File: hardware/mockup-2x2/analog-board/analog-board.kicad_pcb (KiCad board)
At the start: 4 copper layers, 100 x 62 mm, 135 parts, among them J1 12V, J2 COIL JOINT, J4 MCU, J5 PI ZERO, Q1 AO3401A, Q11 AO3400A, Q12 AO3400A, Q13 AO3400A, Q14 AO3400A, Q2 AO3400A, Q21 AO3401A, Q22 AO3401A, Q23 AO3401A, Q24 AO3401A, U1 TPS62150, U2 LP2985-5.0, U3 74HC4052, U4 AD8421, U5 OPA2810, U6 OPA2810, U7 ADuM1201

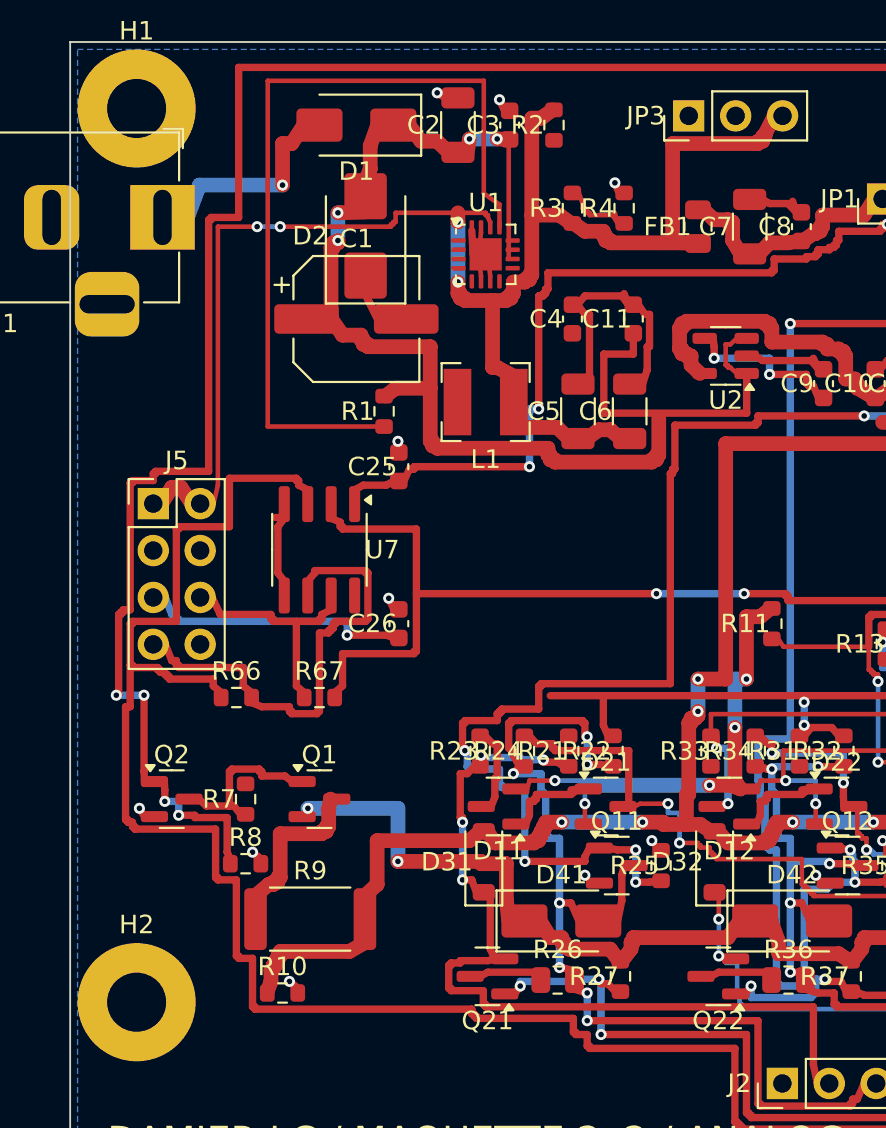
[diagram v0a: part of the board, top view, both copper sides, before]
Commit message: Carte analogique de reference : 18 restes contre 23, artefacts a jour
Generation finale avec les trois seeds nord ouest : 464 pistes, 242
vias, DRC zero, BUCK_SS, BUCK_DEF et la broche isolateur PI_3V3
desormais fermes sans deplacement d'autres nets. Gerbers, placements
JLC et rendu regeneres ; le README de la carte porte la liste de
finition exacte (quatre liaisons jamais routees et les morceaux a
raccorder) et la note de methode sur la saturation locale du routage.
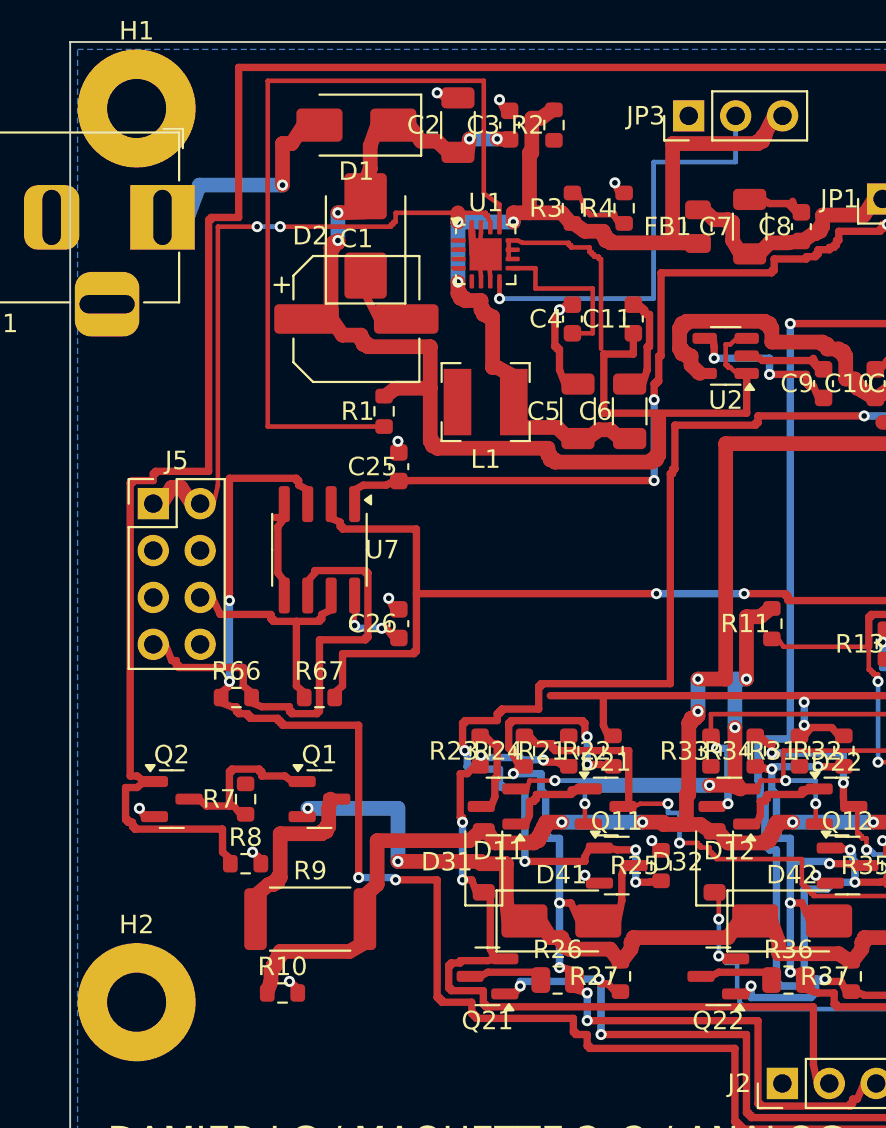
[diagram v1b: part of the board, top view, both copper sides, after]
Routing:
- net BUCK_DEF: track 0.00 -> 23.6 mm, vias 0 -> 1
- net MCU_TX: track 186.2 -> 168.7 mm, vias 1 -> 5
- net PI_3V3: track 14.2 -> 3.66 mm, vias 1 -> 2
- net BUCK_SS: track 0.00 -> 8.96 mm
- net VIN: track 143.8 -> 148.7 mm
- net GND: track 71.0 -> 67.3 mm, vias 24 -> 25
- net 5V_BUCK: track 85.1 -> 83.0 mm, vias 4 -> 5
- net PULSE_EN: track 118.0 -> 119.2 mm, vias 5 -> 1

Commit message: Carte de reference avec passe de finition : 9 restes contre 18
Regeneration des artefacts : 480 pistes, 249 vias, DRC zero, 9
jonctions posees par la finition. VIN, SW, BUCK_PG, BUCK_SS,
BUCK_DEF, 5VA et PI_3V3 sont desormais entiers ; restent cinq nets a
fermer dans pcbnew (M1_A, C2_A, C3_B, BUCK_FB, VREF), leurs couloirs
etant reellement occupes, verification geometrique a l'appui. README
de la carte mis a jour, gerbers, placements JLC et rendu regeneres.
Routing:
- net VIN: track 148.7 -> 185.9 mm
- net 5VA: track 176.1 -> 210.0 mm, vias 17 -> 20
- net PI_3V3: track 3.66 -> 18.2 mm
- net BUCK_PG: track 0.00 -> 14.0 mm, vias 0 -> 2
- net SW: track 0.00 -> 9.71 mm, vias 0 -> 2
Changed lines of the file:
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@@
     (pad "1" thru_hole circle (at 0 0) (size 6.4 6.4) (drill 3.2) (layers *.Cu *.Mask) (net 2 "GND"))
-  )
-  (zone (net 2) (net_name "GND") (layer "B.Cu") (hatch edge 0.5)
-    (connect_pads yes (clearance 0.3))
-    (min_thickness 0.2) (filled_areas_thickness no)
-    (fill yes (thermal_gap 0.3) (thermal_bridge_width 0.4))
-    (polygon (pts (xy 0.4 0.4) (xy 99.6 0.4) (xy 99.6 61.6) (xy 0.4 61.6)))
-  )
-  (gr_rect (start 0 0) (end 100 62) (stroke (width 0.1) (type solid)) (fill none) (layer "Edge.Cuts"))
-  (gr_text "DAMIER LC / MAQUETTE 2x2 / ANALOG" (at 22 59.5) (layer "F.SilkS")
-    (effects (font (size 1.5 1.5) (thickness 0.2)))
-  )
-  (gr_text "vers carte bobines" (at 80 59.5) (layer "F.SilkS")
-    (effects (font (size 1.2 1.2) (thickness 0.2)))
   )
   (segment (start 26 35.4) (end 44.5 35.4) (width 0.4) (layer "F.Cu") (net 21))
@@
   (segment (start 36.125 51.625) (end 36.125 49.875) (width 0.25) (layer "B.Cu") (net 28))
   (segment (start 36.125 49.875) (end 35.5 49.875) (width 0.25) (layer "B.Cu") (net 28))
+  (segment (start 59.129743 23.942133) (end 59.129743 25.142133) (width 0.25) (layer "F.Cu") (net 14))
+  (segment (start 59.129743 25.142133) (end 59.129743 31.305) (width 0.25) (layer "B.Cu") (net 14))
+  (segment (start 59.129743 31.305) (end 61.25 31.305) (width 0.25) (layer "B.Cu") (net 14))
+  (segment (start 63.05 33.105) (end 61.25 31.305) (width 0.25) (layer "F.Cu") (net 14))
+  (segment (start 38.275 31.075) (end 40.075 31.075) (width 0.25) (layer "F.Cu") (net 14))
+  (segment (start 40.075 31.075) (end 40.075 18.991294) (width 0.25) (layer "B.Cu") (net 14))
+  (segment (start 40.075 18.991294) (end 47.277772 18.991294) (width 0.25) (layer "B.Cu") (net 14))
+  (segment (start 47.277772 18.991294) (end 47.277772 19.707588) (width 0.25) (layer "B.Cu") (net 14))
+  (segment (start 25.725 5.725) (end 26.225 6.225) (width 0.25) (layer "F.Cu") (net 5))
+  (segment (start 26.225 6.225) (end 19.875 6.225) (width 0.25) (layer "B.Cu") (net 5))
+  (segment (start 19.875 6.225) (end 19.875 12.375) (width 0.25) (layer "B.Cu") (net 5))
+  (segment (start 20.675 12.375) (end 19.875 12.375) (width 0.25) (layer "F.Cu") (net 5))
+  (segment (start 15.101445 31.570595) (end 15.101445 28.850297) (width 0.25) (layer "B.Cu") (net 73))
+  (segment (start 15.101445 28.850297) (end 5.35 28.850297) (width 0.25) (layer "B.Cu") (net 73))
+  (segment (start 5.35 28.850297) (end 5.35 30.93) (width 0.25) (layer "B.Cu") (net 73))
+  (segment (start 20.65 10.65) (end 20.675 11.375) (width 0.25) (layer "F.Cu") (net 4))
+  (segment (start 20.679308 11.499926) (end 20.679308 11.625) (width 0.25) (layer "F.Cu") (net 4))
+  (segment (start 20.534463 10.926569) (end 18.734463 10.926569) (width 0.25) (layer "F.Cu") (net 4))
+  (segment (start 18.734463 10.926569) (end 20.65 17.2) (width 0.25) (layer "B.Cu") (net 4))
+  (segment (start 20.65 17.7) (end 20.65 17.2) (width 0.25) (layer "F.Cu") (net 4))
+  (segment (start 9.975 40.575) (end 11.825 41.65) (width 0.25) (layer "F.Cu") (net 3))
+  (segment (start 14.5 11.15) (end 14.5 27.085967) (width 0.25) (layer "B.Cu") (net 3))
+  (segment (start 14.5 27.085967) (end 18.15 27.085967) (width 0.25) (layer "B.Cu") (net 3))
+  (segment (start 18.15 27.085967) (end 18.15 42.621934) (width 0.25) (layer "B.Cu") (net 3))
   (via (at 44.5 35.4) (size 0.6) (drill 0.3) (layers "F.Cu" "B.Cu") (net 21))
   (via (at 53 35.4) (size 0.6) (drill 0.3) (layers "F.Cu" "B.Cu") (net 21))
@@
   (via (at 35.125 47.5) (size 0.6) (drill 0.3) (layers "F.Cu" "B.Cu") (net 28))
   (via (at 35.125 49.5) (size 0.6) (drill 0.3) (layers "F.Cu" "B.Cu") (net 28))
+  (via (at 59.129743 25.142133) (size 0.6) (drill 0.3) (layers "F.Cu" "B.Cu") (net 14))
+  (via (at 61.25 31.305) (size 0.6) (drill 0.3) (layers "F.Cu" "B.Cu") (net 14))
+  (via (at 40.075 31.075) (size 0.6) (drill 0.3) (layers "F.Cu" "B.Cu") (net 14))
+  (via (at 26.225 6.225) (size 0.6) (drill 0.3) (layers "F.Cu" "B.Cu") (net 5))
+  (via (at 19.875 12.375) (size 0.6) (drill 0.3) (layers "F.Cu" "B.Cu") (net 5))
+  (via (at 18.734463 10.926569) (size 0.6) (drill 0.3) (layers "F.Cu" "B.Cu") (net 4))
+  (via (at 20.65 17.2) (size 0.6) (drill 0.3) (layers "F.Cu" "B.Cu") (net 4))
+  (zone (net 2) (net_name "GND") (layer "B.Cu") (hatch edge 0.5)
+    (connect_pads yes (clearance 0.3))
+    (min_thickness 0.2) (filled_areas_thickness no)
+    (fill yes (thermal_gap 0.3) (thermal_bridge_width 0.4))
+    (polygon (pts (xy 0.4 0.4) (xy 99.6 0.4) (xy 99.6 61.6) (xy 0.4 61.6)))
+  )
+  (gr_rect (start 0 0) (end 100 62) (stroke (width 0.1) (type solid)) (fill none) (layer "Edge.Cuts"))
+  (gr_text "DAMIER LC / MAQUETTE 2x2 / ANALOG" (at 22 59.5) (layer "F.SilkS")
+    (effects (font (size 1.5 1.5) (thickness 0.2)))
+  )
+  (gr_text "vers carte bobines" (at 80 59.5) (layer "F.SilkS")
+    (effects (font (size 1.2 1.2) (thickness 0.2)))
+  )
 )

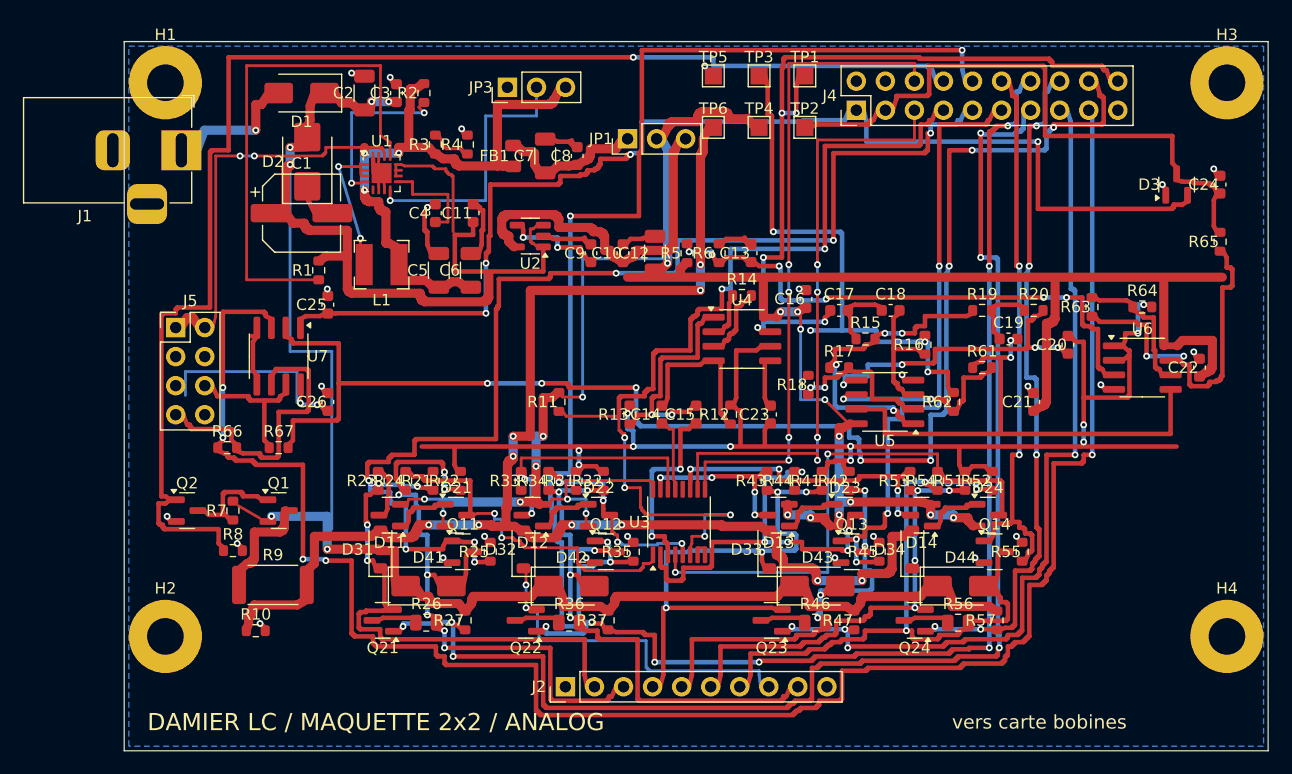
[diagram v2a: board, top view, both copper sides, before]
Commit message: Reference LED complete : cartes, gabarit bois, protocole, docs
Carte analogique regeneree avec le tampon deplace pres du connecteur
MCU : les nets LED (donnees, tampon, 5V vers le joint 12 broches)
sont entierement routes, 499 pistes, 259 vias, DRC zero, 12 jonctions
de finition posees ; restent les sept couloirs satures connus de la
bande des cellules et du coin buck, listes dans le README de la
carte. Gabarit de percage surface-template (contour carte, visserie,
deux points lumineux par case) genere par la mecanique et exporte.
Protocole : M10 bois contre acrylique, M11 bruit des LED. ADR 0009
(LED de camp et surface bois) indexe, READMEs et fiche
d'approvisionnement mis a jour (lignes WS2812B et tampon, assemblage
des deux cartes, totaux revises, contreplaque au lieu d'acrylique).
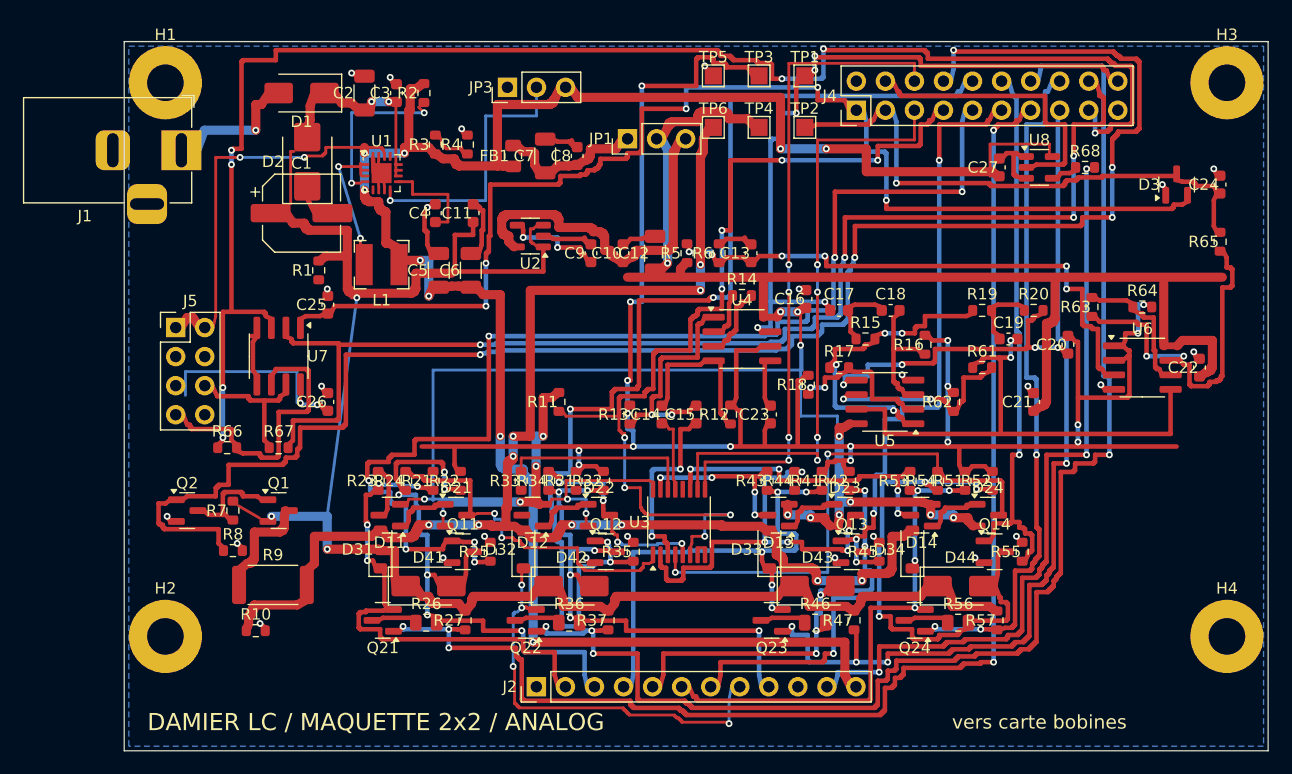
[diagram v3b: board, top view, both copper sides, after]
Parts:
- added C27: 100n, Capacitor_SMD:C_0603_1608Metric, F.Cu at (76.5, 11.0)
- added R68: 470, Resistor_SMD:R_0603_1608Metric, F.Cu at (84.0, 11.0)
- added U8: 74AHCT1G125, Package_TO_SOT_SMD:SOT-23-5, F.Cu at (80.0, 11.0)
- J2: footprint Connector_PinHeader_2.54mm:PinHeader_1x10_P2.54mm_Vertical -> Connector_PinHeader_2.54mm:PinHeader_1x12_P2.54mm_Vertical
- moved J2 2.54 mm to (36.0, 56.4)
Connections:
- J4 pad 4: GND -> LED_DIN
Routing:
- net 5V_BUCK: track 83.0 -> 206.2 mm, vias 5 -> 11
- net LED_DIN5: track 0.00 -> 67.8 mm, vias 0 -> 3
- net BUCK_EN: track 45.1 -> 0.00 mm
- net PULSE_EN: track 119.2 -> 152.2 mm, vias 1 -> 5
- net MCU_TX: track 168.7 -> 135.9 mm, vias 5 -> 7
- net VIN: track 185.9 -> 158.0 mm, vias 6 -> 5
- net DAMP2_N: track 97.0 -> 122.0 mm, vias 7 -> 4
- net 5VA: track 210.0 -> 235.0 mm, vias 20 -> 18
- net LED_DIN: track 0.00 -> 25.0 mm
- net MCU_RX: track 125.3 -> 108.4 mm, vias 8 -> 4
- net VREF: track 170.7 -> 185.2 mm, vias 15 -> 17
- net C4_B: track 58.0 -> 66.1 mm, vias 3 -> 4
- net INA_OUT: track 67.6 -> 61.0 mm
- net C2_A: track 30.7 -> 36.9 mm, vias 2 -> 4
- net DRIVE2: track 104.3 -> 98.8 mm
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
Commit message: Carte analogique de maquette : les vingt-huit liaisons fermées
Le compte du build disait sept liaisons ouvertes, KiCad en comptait
vingt-huit. L'arbitre était faux : le modèle de connexité ignorait la
masse, fusionnait les deux couches sans exiger de via et prenait la
boîte d'une pastille pour son cuivre. Il est remplacé par le modèle
exact du quadrant, forme vraie des pastilles comprise, avec le plan de
masse calculé comme le calcule le remplisseur de KiCad, îlot par îlot.
Le compte du build est désormais celui de KiCad, vérifié sur l'ancien
fichier comme sur le nouveau.

Dix-neuf des vingt-huit manquants étaient des masses : des groupes de
pastilles reliés en face avant mais jamais descendus vers un îlot que
le plan garde entier. Une passe de finition de la masse, jouée contre
les îlots réels, les ferme ; elle ne déplace pas le plan, puisque le
cuivre de masse n'est pas étranger au sien.

Pour le reste, deux outils. Un labyrinthe à géométrie exacte, trame de
0,05 mm sur les deux couches, via et coude payants, qui ferme ce
qu'aucun raccord droit ne ferme, dont une nappe de 25 mm. Et treize
routes structurelles tracées avant le routage dans des canaux mesurés
libres de pastilles, chacune revérifiée au build : les deux lignes de
cellule, la prise A de la cellule 2, deux broches du multiplexeur, la
résistance de fuite de la cellule 1, les deux sorties du régulateur, et
quatre masses que le plan n'atteint pas, dont un bus le long du bord
sud pour le connecteur de bobines.

La garde des raccords passe de 0,132 à 0,15 mm, la valeur de la classe
de nets : le DRC de KiCad comptait les 0,138 comme des erreurs.

Résultat mesuré : 557 pistes, 296 vias, zéro élément non connecté au
DRC de KiCad comme au compte du build. Restent deux défauts de
placement, hérités et documentés : 49 chevauchements de courtyard et
la broche 2 du jack J1, 1 mm hors du contour.
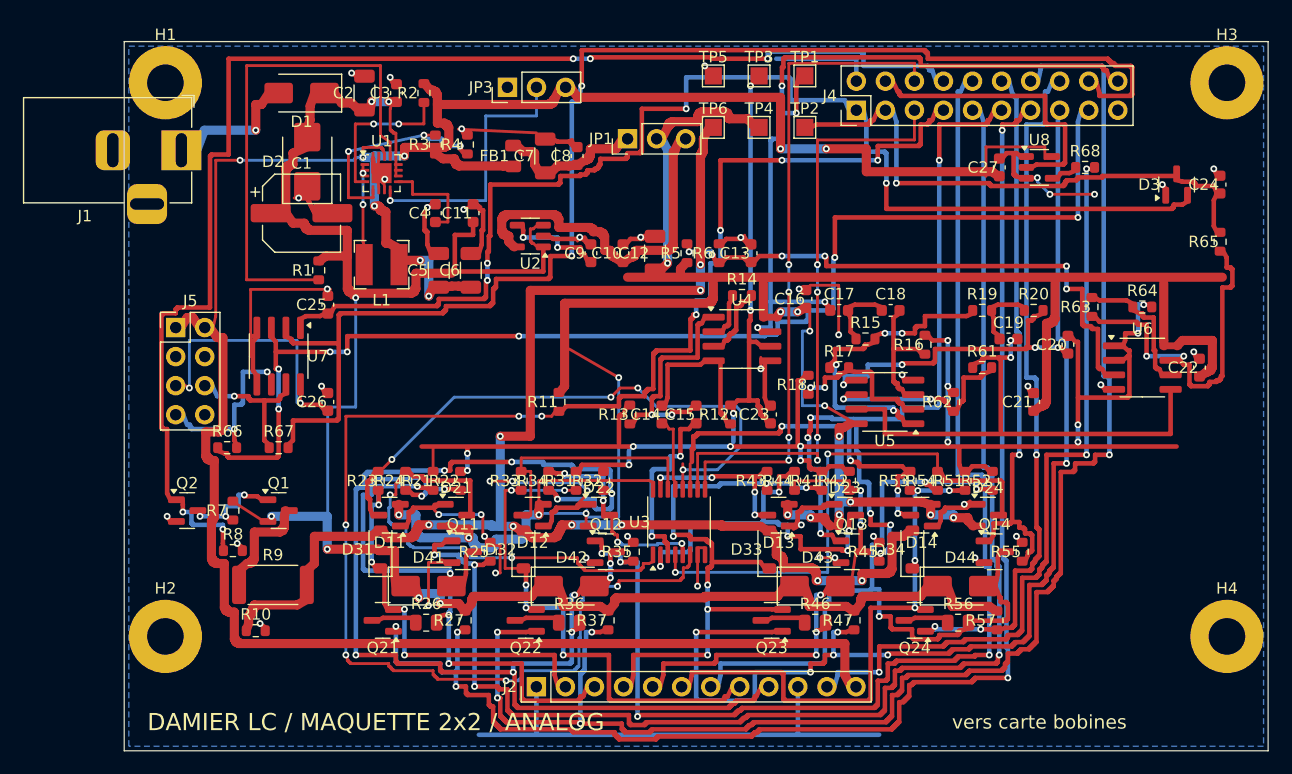
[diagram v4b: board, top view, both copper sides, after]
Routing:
- net GND: track 71.8 -> 191.0 mm, vias 25 -> 46
- net C2_B: track 44.0 -> 109.3 mm, vias 6 -> 10
- net MUX_INH: track 84.0 -> 140.6 mm, vias 8 -> 10
- net M1_A: track 4.40 -> 50.8 mm, vias 0 -> 4
- net BUCK_EN: track 0.00 -> 45.1 mm
- net PULSE_EN: track 152.2 -> 117.7 mm
- net MCU_TX: track 135.9 -> 108.0 mm
- net 5V_BUCK: track 206.2 -> 229.9 mm, vias 11 -> 8
- net DAMP3_N: track 79.5 -> 101.3 mm, vias 4 -> 6
- net DRIVE1: track 102.1 -> 122.7 mm, vias 7 -> 4
- net DAMP2_N: track 122.0 -> 140.9 mm, vias 4 -> 5
- net DRIVE3: track 53.8 -> 72.6 mm, vias 4 -> 7
- net BUCK_FB: track 3.98 -> 18.9 mm, vias 0 -> 3
- net VREF: track 185.2 -> 170.8 mm
- net MCU_RX: track 108.4 -> 121.3 mm, vias 4 -> 2
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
